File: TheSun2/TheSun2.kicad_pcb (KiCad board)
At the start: 2 copper layers, 65 x 30 mm, 12 parts, among them J1 , J2 , J3 , Q1 IRFZ44N, Q2 IRFZ44N

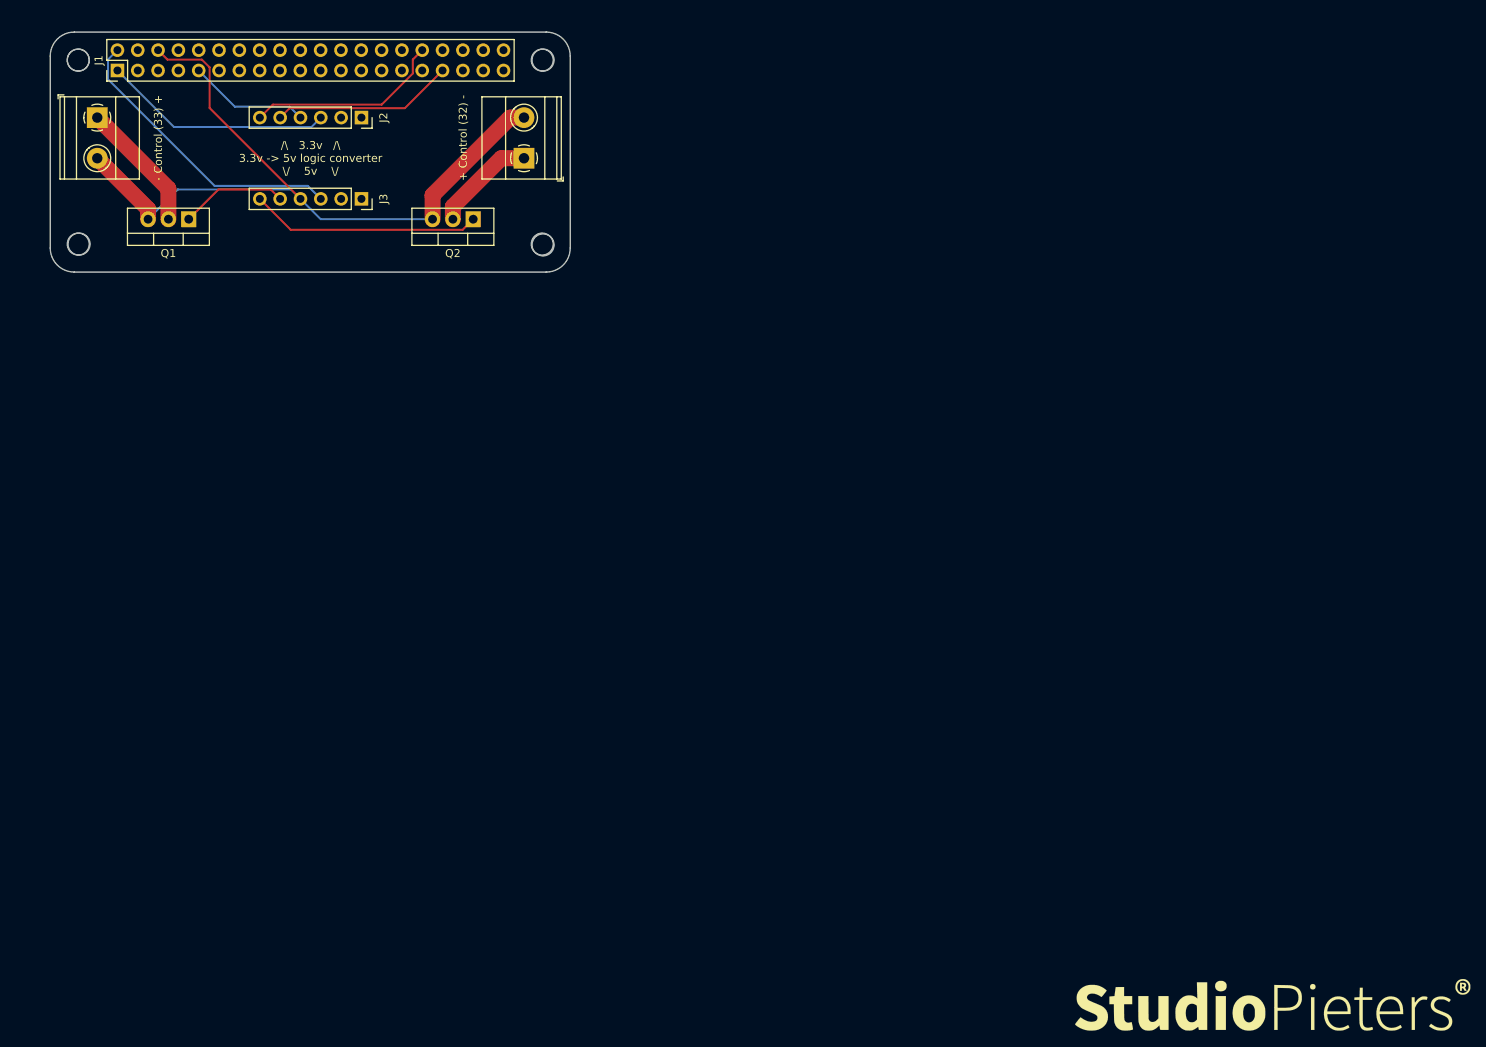
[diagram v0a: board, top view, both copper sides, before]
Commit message: Added fancy pi power mosfet hat
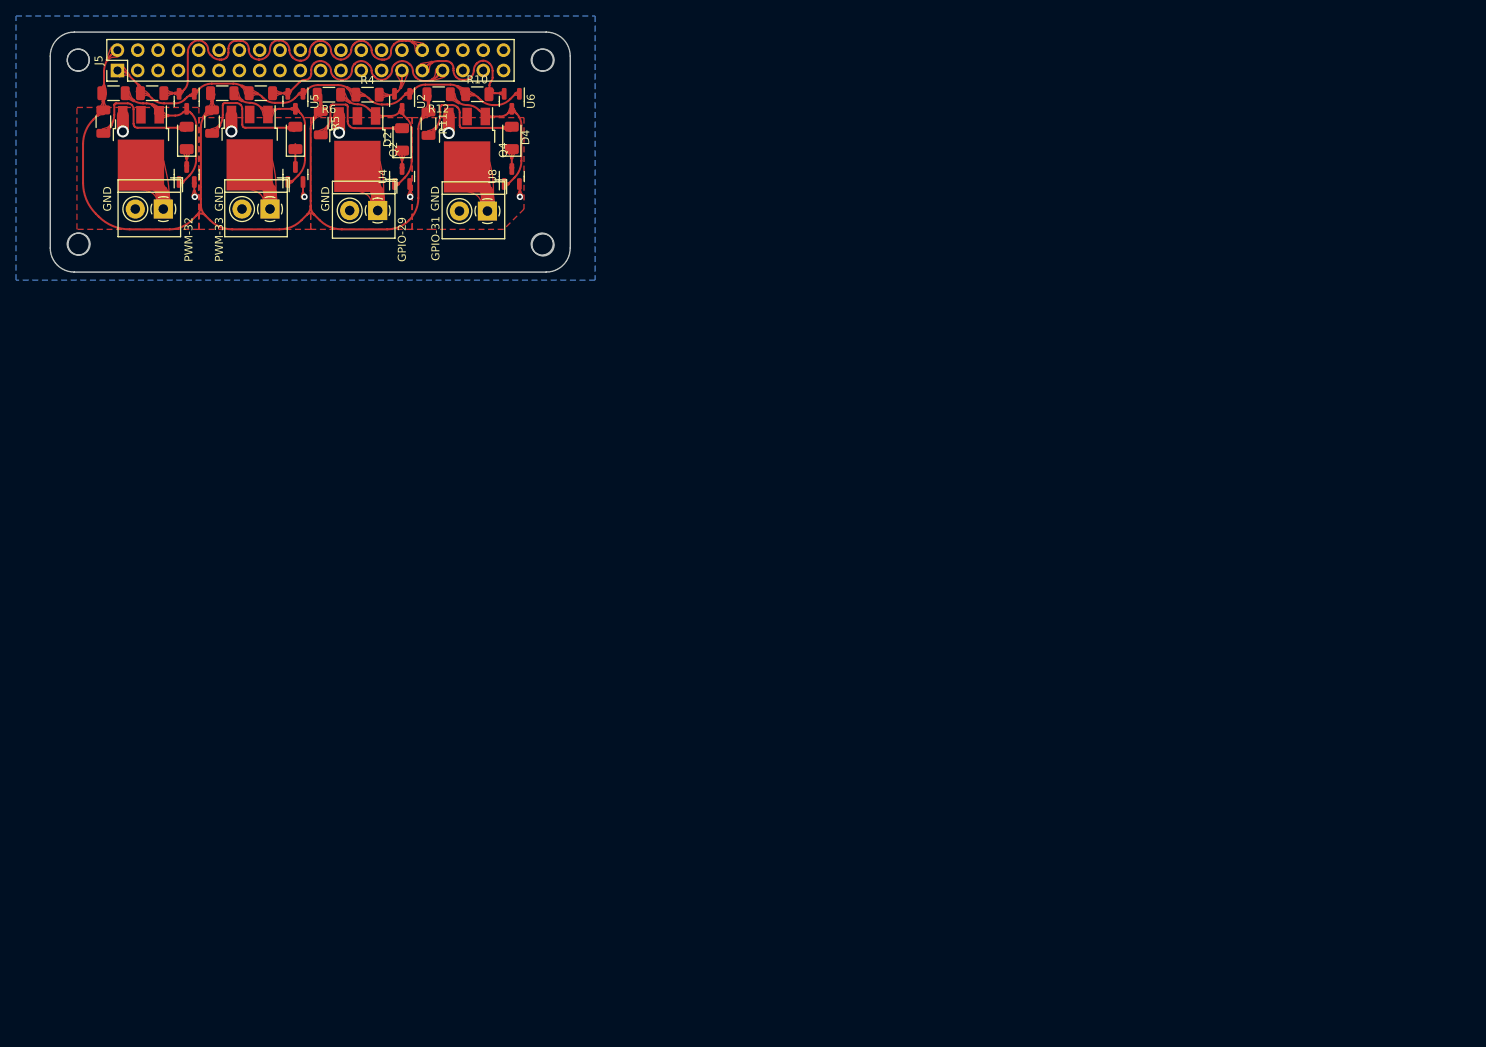
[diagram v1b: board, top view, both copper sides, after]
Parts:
- removed + Control (32) -: , TerminalBlock_Phoenix:TerminalBlock_Phoenix_MKDS-1,5-2-5.08_1x02_P5.08mm_Horizontal
- removed - Control (33) +: , TerminalBlock_Phoenix:TerminalBlock_Phoenix_MKDS-1,5-2-5.08_1x02_P5.08mm_Horizontal
- removed G***: LOGO, StudioPieters:StudioPieters_Kicad_Logo
- removed J1: , Connector_PinHeader_2.54mm:PinHeader_2x20_P2.54mm_Vertical
- removed J2, J3: , Connector_PinSocket_2.54mm:PinSocket_1x06_P2.54mm_Vertical
- added D1: LED, LED_SMD:LED_1206_3216Metric, F.Cu at (67.1, 62.2)
- added D2: LED, LED_SMD:LED_1206_3216Metric, F.Cu at (94.0, 62.4)
- added D3: LED, LED_SMD:LED_1206_3216Metric, F.Cu at (80.6, 62.2)
- added D4: LED, LED_SMD:LED_1206_3216Metric, F.Cu at (107.7, 62.2)
- added GPIO-29: Screw_Terminal_01x02, TerminalBlock_4Ucon:TerminalBlock_4Ucon_1x02_P3.50mm_Horizontal, F.Cu at (90.9, 71.3)
- added GPIO-31: Screw_Terminal_01x02, TerminalBlock_4Ucon:TerminalBlock_4Ucon_1x02_P3.50mm_Horizontal, F.Cu at (104.6, 71.4)
- added J5: Conn_02x20_Odd_Even, Connector_PinHeader_2.54mm:PinHeader_2x20_P2.54mm_Vertical, F.Cu at (58.4, 53.8)
- added PWM-32: Screw_Terminal_01x02, TerminalBlock_4Ucon:TerminalBlock_4Ucon_1x02_P3.50mm_Horizontal, F.Cu at (64.1, 71.1)
- added PWM-33: Screw_Terminal_01x02, TerminalBlock_4Ucon:TerminalBlock_4Ucon_1x02_P3.50mm_Horizontal, F.Cu at (77.5, 71.1)
- added Q3: IRLR7843, Package_TO_SOT_SMD:TO-252-3_TabPin2, F.Cu at (74.9, 63.5)
- added Q4: IRLR7843, Package_TO_SOT_SMD:TO-252-3_TabPin2, F.Cu at (102.1, 63.8)
- added R1: 10K, Resistor_SMD:R_1206_3216Metric, F.Cu at (62.7, 56.6)
- added R10: 10K, Resistor_SMD:R_1206_3216Metric, F.Cu at (103.4, 56.8)
- added R11: 500R, Resistor_SMD:R_1206_3216Metric, F.Cu at (97.3, 60.5)
- added R12: 10K, Resistor_SMD:R_1206_3216Metric, F.Cu at (98.6, 56.8)
- added R2: 500R, Resistor_SMD:R_1206_3216Metric, F.Cu at (56.6, 60.2)
- added R3: 10K, Resistor_SMD:R_1206_3216Metric, F.Cu at (57.9, 56.6)
- added R4: 10K, Resistor_SMD:R_1206_3216Metric, F.Cu at (89.7, 56.8)
- added R5: 500R, Resistor_SMD:R_1206_3216Metric, F.Cu at (83.8, 60.4)
- added R6: 10K, Resistor_SMD:R_1206_3216Metric, F.Cu at (84.8, 56.8)
- added R7: 10K, Resistor_SMD:R_1206_3216Metric, F.Cu at (76.3, 56.6)
- added R8: 500R, Resistor_SMD:R_1206_3216Metric, F.Cu at (70.2, 60.2)
- added R9: 10K, Resistor_SMD:R_1206_3216Metric, F.Cu at (71.5, 56.6)
- added U1: 2N7002H, Package_TO_SOT_SMD:SOT-23, F.Cu at (67.1, 57.7)
- added U2: 2N7002H, Package_TO_SOT_SMD:SOT-23, F.Cu at (94.0, 57.7)
- added U3: 2N7002H, Package_TO_SOT_SMD:SOT-23, F.Cu at (67.1, 66.8)
- added U4: 2N7002H, Package_TO_SOT_SMD:SOT-23, F.Cu at (94.0, 67.1)
- added U5: 2N7002H, Package_TO_SOT_SMD:SOT-23, F.Cu at (80.6, 57.7)
- added U6: 2N7002H, Package_TO_SOT_SMD:SOT-23, F.Cu at (107.7, 57.7)
- added U7: 2N7002H, Package_TO_SOT_SMD:SOT-23, F.Cu at (80.6, 66.8)
- added U8: 2N7002H, Package_TO_SOT_SMD:SOT-23, F.Cu at (107.7, 67.1)
- Q1, Q2: value IRFZ44N -> IRLR7843; footprint Package_TO_SOT_THT:TO-220-3_Vertical -> Package_TO_SOT_SMD:TO-252-3_TabPin2
- moved Q2 16.9 mm to (88.4, 63.7), turned to -90 degrees
- moved Q1 10.7 mm to (61.3, 63.5), turned to -90 degrees
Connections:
- net Net-(J1-Pad6) renamed GND
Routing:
- net 5v: track 0.00 -> 115.7 mm
- net GND: track 95.8 -> 14.5 mm, vias 0 -> 8
- net 3.3v: track 0.00 -> 57.2 mm
- net /PWM-32: track 0.00 -> 51.1 mm
- net Net-(J1-Pad2): track 36.9 -> 0.00 mm
- net /PWM-33: track 0.00 -> 30.3 mm
- net Net-(J1-Pad1) (its old number): track 28.8 -> 0.00 mm
- net Net-(J1-Pad32): track 24.8 -> 0.00 mm
- net Net-(J1-Pad33): track 22.7 -> 0.00 mm
- net Net-(Q4-Pad1): track 0.00 -> 19.6 mm
- net Net-(Q3-Pad1): track 0.00 -> 19.5 mm
- net /GPIO-31: track 0.00 -> 17.9 mm
- net Net-(D3-Pad2): track 0.00 -> 15.9 mm
- net Net-(D1-Pad2): track 0.00 -> 15.7 mm
- net Net-(D4-Pad2): track 0.00 -> 15.4 mm
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- added copper zone on B.Cu, net GND
- added copper zone on F.Cu, net Net-(J1-Pad1)
- added copper zone on F.Cu, net Net-(J2-Pad1)
- added copper zone on F.Cu, net Net-(J3-Pad1)
- added copper zone on F.Cu, net Net-(J4-Pad1)
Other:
- net class Default removed
- board text added: "GND"
- board text removed: "/\ 3.3v /\ 3.3v -> 5v logic converter \/ 5v \/"

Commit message: Added silkscreening
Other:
- board text added: "+"
- board text added: "30v Max, 0.0033R VCC -> Load -> Terminal+"
- board text added: "Barnaby Parker 2022"
- board text added: "Pi Mosfet Hat"
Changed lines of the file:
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@@
     (property "Sheetname" "")
     (attr smd)
-    (fp_text reference "R12" (at 0 -1.82) (layer "F.SilkS")
+    (fp_text reference "R12" (at 0 -1.82) (layer "F.SilkS") hide
       (effects (font (size 1 1) (thickness 0.15)))
     )
@@
     (property "Sheetname" "")
     (attr smd)
-    (fp_text reference "Q2" (at 0 -4.5 90) (layer "F.SilkS")
+    (fp_text reference "Q2" (at 0 -4.5 90) (layer "F.SilkS") hide
       (effects (font (size 1 1) (thickness 0.15)))
     )
@@
     (property "Sheetname" "")
     (attr smd)
-    (fp_text reference "D4" (at 0.06 1.72 90) (layer "F.SilkS")
+    (fp_text reference "D4" (at 0.06 1.72 90) (layer "F.SilkS") hide
       (effects (font (size 1 1) (thickness 0.15)))
     )
@@
     (property "Sheetname" "")
     (attr smd)
-    (fp_text reference "U2" (at 0 -2.4 90) (layer "F.SilkS")
+    (fp_text reference "U2" (at 0 -2.4 90) (layer "F.SilkS") hide
       (effects (font (size 1 1) (thickness 0.15)))
     )
@@
     (property "Sheetname" "")
     (attr smd)
-    (fp_text reference "R6" (at 0 -1.82) (layer "F.SilkS")
+    (fp_text reference "R6" (at 0 -1.82) (layer "F.SilkS") hide
       (effects (font (size 1 1) (thickness 0.15)))
     )
@@
     (property "Sheetname" "")
     (attr smd)
-    (fp_text reference "U6" (at 0 -2.4 90) (layer "F.SilkS")
+    (fp_text reference "U6" (at 0 -2.4 90) (layer "F.SilkS") hide
       (effects (font (size 1 1) (thickness 0.15)))
     )
@@
     (property "Sheetname" "")
     (attr smd)
-    (fp_text reference "R10" (at 0 -1.82) (layer "F.SilkS")
+    (fp_text reference "R10" (at 0 -1.82) (layer "F.SilkS") hide
       (effects (font (size 1 1) (thickness 0.15)))
     )
@@
     (property "Sheetname" "")
     (attr smd)
-    (fp_text reference "U4" (at 0 -2.4 90) (layer "F.SilkS")
+    (fp_text reference "U4" (at 0 -2.4 90) (layer "F.SilkS") hide
       (effects (font (size 1 1) (thickness 0.15)))
     )
@@
     (property "Sheetname" "")
     (attr smd)
-    (fp_text reference "R4" (at 0 -1.82) (layer "F.SilkS")
+    (fp_text reference "R4" (at 0 -1.82) (layer "F.SilkS") hide
       (effects (font (size 1 1) (thickness 0.15)))
     )
@@
     (property "Sheetname" "")
     (attr smd)
-    (fp_text reference "R5" (at 0 -1.82 90) (layer "F.SilkS")
+    (fp_text reference "R5" (at 0 -1.82 90) (layer "F.SilkS") hide
       (effects (font (size 1 1) (thickness 0.15)))
     )
@@
     (property "Sheetname" "")
     (attr smd)
-    (fp_text reference "U5" (at 0 -2.4 90) (layer "F.SilkS")
+    (fp_text reference "U5" (at 0 -2.4 90) (layer "F.SilkS") hide
       (effects (font (size 1 1) (thickness 0.15)))
     )
@@
     (property "Sheetname" "")
     (attr smd)
-    (fp_text reference "Q4" (at 0 -4.5 90) (layer "F.SilkS")
+    (fp_text reference "Q4" (at 0 -4.5 90) (layer "F.SilkS") hide
       (effects (font (size 1 1) (thickness 0.15)))
     )
@@
     (property "Sheetname" "")
     (attr smd)
-    (fp_text reference "D2" (at 0 -1.82 90) (layer "F.SilkS")
+    (fp_text reference "D2" (at 0 -1.82 90) (layer "F.SilkS") hide
       (effects (font (size 1 1) (thickness 0.15)))
     )
@@
     (property "Sheetname" "")
     (attr smd)
-    (fp_text reference "U8" (at 0 -2.4 90) (layer "F.SilkS")
+    (fp_text reference "U8" (at 0 -2.4 90) (layer "F.SilkS") hide
       (effects (font (size 1 1) (thickness 0.15)))
     )
@@
     (property "Sheetname" "")
     (attr through_hole)
-    (fp_text reference "J5" (at 1.27 -2.33 90) (layer "F.SilkS")
+    (fp_text reference "J5" (at 1.27 -2.33 90) (layer "F.SilkS") hide
       (effects (font (size 1 1) (thickness 0.15)))
     )
@@
     (property "Sheetname" "")
     (attr smd)
-    (fp_text reference "R11" (at 0 -1.82 90) (layer "F.SilkS")
+    (fp_text reference "R11" (at 0 -1.82 90) (layer "F.SilkS") hide
       (effects (font (size 1 1) (thickness 0.15)))
     )
@@
   (gr_circle (center 111.5 52.5) (end 114.5 52.5) (layer "F.CrtYd") (width 0.05) (fill none))
   (gr_circle (center 53.5 52.5) (end 56.5 52.5) (layer "F.CrtYd") (width 0.05) (fill none))
+  (gr_text "30v Max, 0.0033R\nVCC -> Load -> Terminal+ " (at 82.296 65.659) (layer "B.SilkS")
+    (effects (font (size 1.5 1.5) (thickness 0.3)) (justify mirror))
+  )
+  (gr_text "Barnaby Parker 2022" (at 112.395 64.135 90) (layer "F.SilkS")
+    (effects (font (size 1 1) (thickness 0.2)))
+  )
+  (gr_text "+" (at 93.98 69.977) (layer "F.SilkS")
+    (effects (font (size 1 1) (thickness 0.15)))
+  )
   (gr_text "GND" (at 71.12 69.85 90) (layer "F.SilkS")
     (effects (font (size 1 1) (thickness 0.15)))
@@
     (effects (font (size 1 1) (thickness 0.15)))
   )
+  (gr_text "Pi Mosfet Hat" (at 52.07 64.135 90) (layer "F.SilkS")
+    (effects (font (size 1.5 1.5) (thickness 0.3)))
+  )
+  (gr_text "+" (at 80.518 69.723) (layer "F.SilkS")
+    (effects (font (size 1 1) (thickness 0.15)))
+  )
+  (gr_text "+" (at 107.696 69.977) (layer "F.SilkS")
+    (effects (font (size 1 1) (thickness 0.15)))
+  )
   (gr_text "GND" (at 84.407368 69.857815 90) (layer "F.SilkS")
     (effects (font (size 1 1) (thickness 0.15)))
   )
+  (gr_text "+" (at 67.056 69.723) (layer "F.SilkS")
+    (effects (font (size 1 1) (thickness 0.15)))
+  )

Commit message: Added first draft for pi mosfethat
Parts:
- added G***: LOGO, LOGO, B.Cu at (82.5, 62.6)
- GPIO-29, GPIO-31, PWM-32, PWM-33: footprint TerminalBlock_4Ucon:TerminalBlock_4Ucon_1x02_P3.50mm_Horizontal -> BSP-Custom:TerminalBlock_4Ucon_1x02_P3.50mm_Horizontal
- moved PWM-32 0.19 mm to (64.1, 71.3)
- moved PWM-33 0.19 mm to (77.5, 71.3)
- moved GPIO-31 0.07 mm to (104.6, 71.3)
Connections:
- PWM-32 pad 1: Net-(Q1-Pad2) -> Net-(J1-Pad1)
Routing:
- net 5v: track 115.7 -> 123.9 mm
- net Net-(J3-Pad1): track 6.46 -> 0.00 mm
- net Net-(J4-Pad1): track 6.46 -> 0.00 mm
- net Net-(J2-Pad1): track 6.40 -> 0.00 mm
- net Net-(J1-Pad1): track 6.16 -> 0.00 mm
